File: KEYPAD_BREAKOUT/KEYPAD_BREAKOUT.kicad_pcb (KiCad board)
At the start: 4 copper layers, 46.7 x 76.6 mm, 21 parts, among them J1 Conn_01x14, SW0 SW_RGB, SW1 SW_RGB, SW2 SW_RGB, SW3 SW_RGB, SW4 SW_RGB, SW5 SW_RGB, SW6 SW_RGB, SW7 SW_RGB, SW8 SW_RGB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

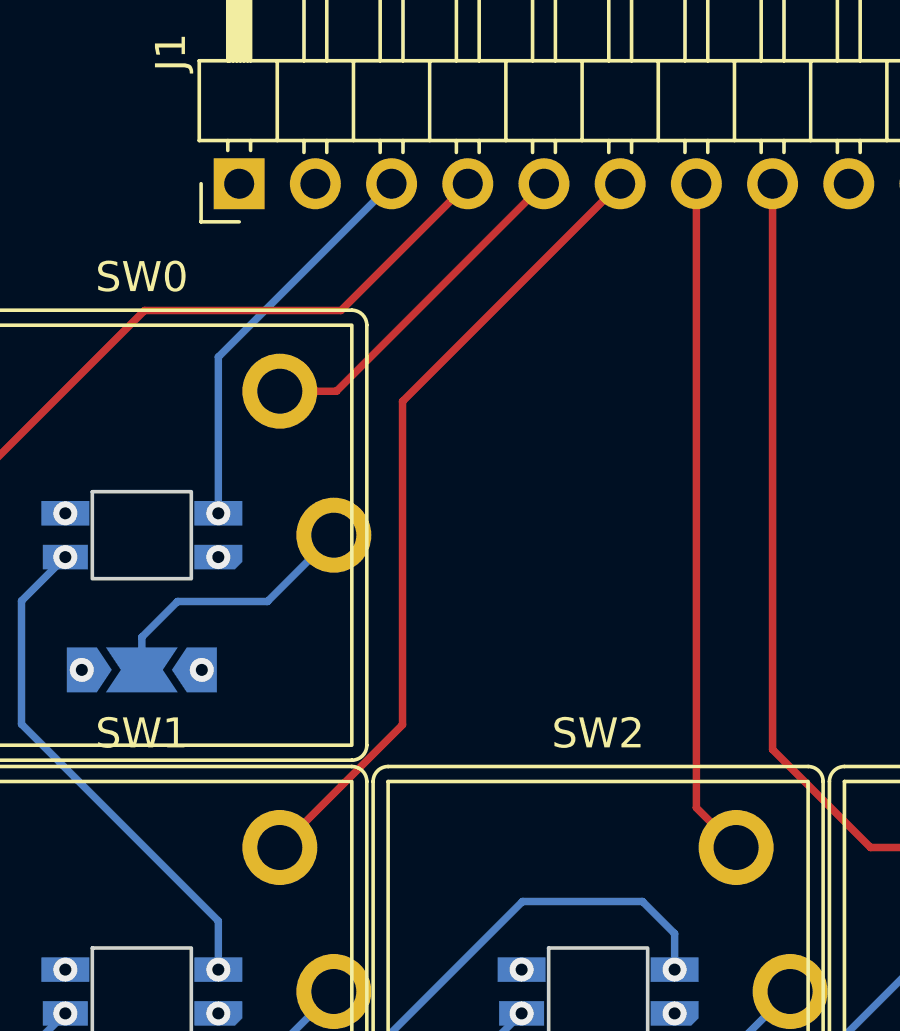
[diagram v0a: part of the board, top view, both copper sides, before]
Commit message: [KEYPAD_BREAKOUT] Minor trace adjust, readme update
Signed-off-by: Adam BZH <424778940z@users.noreply.github.com>
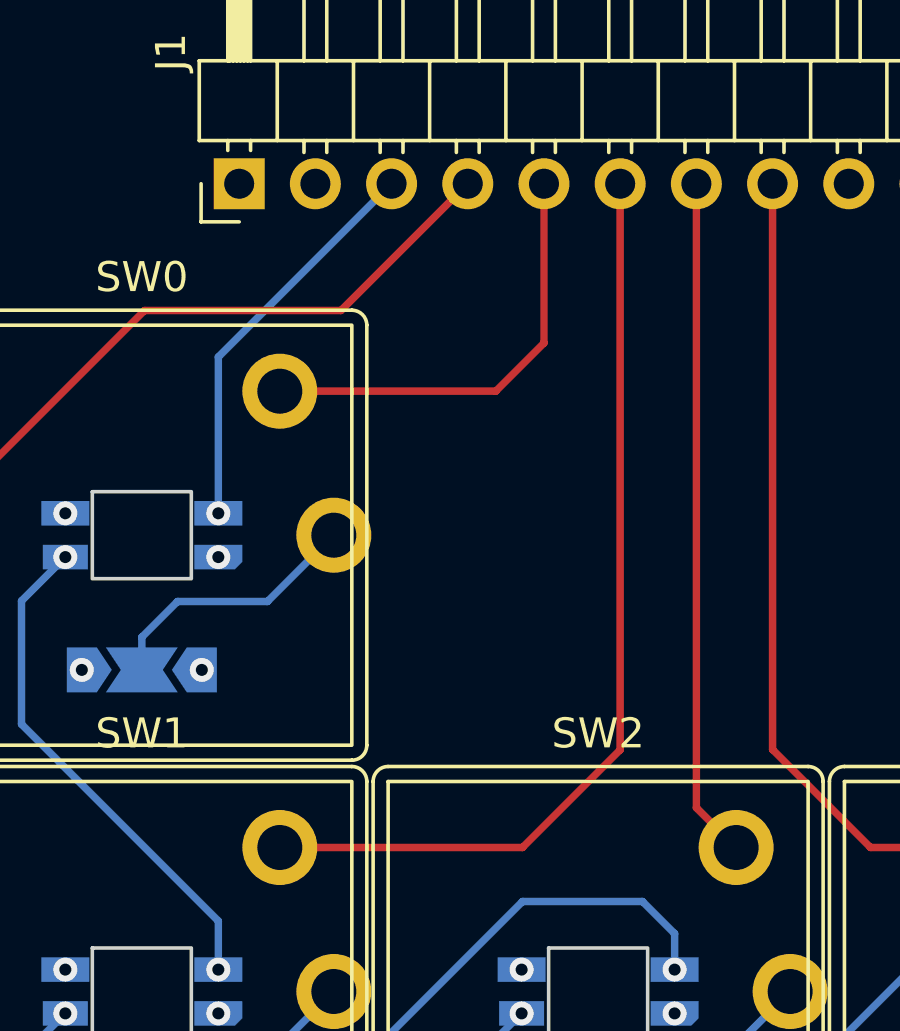
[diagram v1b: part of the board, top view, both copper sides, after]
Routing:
- net /SW1: track 26.8 -> 31.6 mm
- net /SW0: track 11.7 -> 14.8 mm
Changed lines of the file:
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@@
   (segment (start 139.25 100.65) (end 133.4 106.5) (width 0.25) (layer "F.Cu") (net 4))
   (via (at 140.88 100.65) (size 0.8) (drill 0.4) (layers "F.Cu" "B.Cu") (net 4))
-  (segment (start 117.61 49.49) (end 119.5 49.49) (width 0.25) (layer "F.Cu") (net 5))
-  (segment (start 119.5 49.49) (end 126.415 42.575) (width 0.25) (layer "F.Cu") (net 5))
-  (segment (start 121.7 49.83) (end 128.955 42.575) (width 0.25) (layer "F.Cu") (net 6))
-  (segment (start 121.7 60.61) (end 121.7 49.83) (width 0.25) (layer "F.Cu") (net 6))
-  (segment (start 117.61 64.7) (end 121.7 60.61) (width 0.25) (layer "F.Cu") (net 6))
+  (segment (start 126.415 47.885) (end 126.415 42.575) (width 0.25) (layer "F.Cu") (net 5))
+  (segment (start 117.61 49.49) (end 124.81 49.49) (width 0.25) (layer "F.Cu") (net 5))
+  (segment (start 124.81 49.49) (end 126.415 47.885) (width 0.25) (layer "F.Cu") (net 5))
+  (segment (start 125.7 64.7) (end 128.955 61.445) (width 0.25) (layer "F.Cu") (net 6))
+  (segment (start 117.61 64.7) (end 125.7 64.7) (width 0.25) (layer "F.Cu") (net 6))
+  (segment (start 128.955 61.445) (end 128.955 42.575) (width 0.25) (layer "F.Cu") (net 6))
   (segment (start 131.495 63.375) (end 131.495 42.575) (width 0.25) (layer "F.Cu") (net 7))
   (segment (start 132.82 64.7) (end 131.495 63.375) (width 0.25) (layer "F.Cu") (net 7))
@@
   (segment (start 148.03 79.91) (end 148.03 67.93) (width 0.25) (layer "In1.Cu") (net 11))
   (segment (start 141.655 61.555) (end 141.655 42.575) (width 0.25) (layer "In1.Cu") (net 11))
+  (segment (start 122.5 67.9) (end 144.195 46.205) (width 0.25) (layer "In2.Cu") (net 12))
+  (segment (start 144.195 46.205) (end 144.195 42.575) (width 0.25) (layer "In2.Cu") (net 12))
+  (segment (start 122.5 90.23) (end 122.5 67.9) (width 0.25) (layer "In2.Cu") (net 12))
   (segment (start 117.61 95.12) (end 122.5 90.23) (width 0.25) (layer "In2.Cu") (net 12))
-  (segment (start 122.5 90.23) (end 122.5 64.27) (width 0.25) (layer "In2.Cu") (net 12))
-  (segment (start 122.5 64.27) (end 144.195 42.575) (width 0.25) (layer "In2.Cu") (net 12))
+  (segment (start 132.82 83.28) (end 137 79.1) (width 0.25) (layer "In2.Cu") (net 13))
+  (segment (start 146.735 51.265) (end 146.735 42.575) (width 0.25) (layer "In2.Cu") (net 13))
+  (segment (start 137 61) (end 146.735 51.265) (width 0.25) (layer "In2.Cu") (net 13))
   (segment (start 132.82 95.12) (end 132.82 83.28) (width 0.25) (layer "In2.Cu") (net 13))
-  (segment (start 137 79.1) (end 137 52.31) (width 0.25) (layer "In2.Cu") (net 13))
-  (segment (start 137 52.31) (end 146.735 42.575) (width 0.25) (layer "In2.Cu") (net 13))
-  (segment (start 132.82 83.28) (end 137 79.1) (width 0.25) (layer "In2.Cu") (net 13))
-  (segment (start 150.1 45.6) (end 149.275 44.775) (width 0.25) (layer "In2.Cu") (net 14))
-  (segment (start 149.275 44.775) (end 149.275 42.575) (width 0.25) (layer "In2.Cu") (net 14))
+  (segment (start 137 79.1) (end 137 61) (width 0.25) (layer "In2.Cu") (net 13))
+  (segment (start 150.1 63.1) (end 149.275 62.275) (width 0.25) (layer "In2.Cu") (net 14))
+  (segment (start 150 75.6) (end 148 73.6) (width 0.25) (layer "In2.Cu") (net 14))
+  (segment (start 150 81.1) (end 150 75.6) (width 0.25) (layer "In2.Cu") (net 14))
+  (segment (start 150.1 65.9) (end 150.1 63.1) (width 0.25) (layer "In2.Cu") (net 14))
+  (segment (start 148.03 95.12) (end 148.03 83.07) (width 0.25) (layer "In2.Cu") (net 14))
+  (segment (start 148 68) (end 150.1 65.9) (width 0.25) (layer "In2.Cu") (net 14))
   (segment (start 148 73.6) (end 148 68) (width 0.25) (layer "In2.Cu") (net 14))
-  (segment (start 148 68) (end 150.1 65.9) (width 0.25) (layer "In2.Cu") (net 14))
   (segment (start 148.03 83.07) (end 150 81.1) (width 0.25) (layer "In2.Cu") (net 14))
-  (segment (start 150 81.1) (end 150 75.6) (width 0.25) (layer "In2.Cu") (net 14))
-  (segment (start 150 75.6) (end 148 73.6) (width 0.25) (layer "In2.Cu") (net 14))
-  (segment (start 150.1 65.9) (end 150.1 45.6) (width 0.25) (layer "In2.Cu") (net 14))
-  (segment (start 148.03 95.12) (end 148.03 83.07) (width 0.25) (layer "In2.Cu") (net 14))
+  (segment (start 149.275 62.275) (end 149.275 42.575) (width 0.25) (layer "In2.Cu") (net 14))
   (segment (start 114.2 71.71) (end 113.01 72.9) (width 0.25) (layer "B.Cu") (net 15))
   (segment (start 117.2 71.71) (end 114.2 71.71) (width 0.25) (layer "B.Cu") (net 15))

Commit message: [KEYPAD_BREAKOUT] Version 1 release, multiple fixes
Signed-off-by: Adam BZH <424778940z@users.noreply.github.com>
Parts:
- added J0: Conn_01x14, Connector_PinHeader_2.54mm:PinHeader_1x14_P2.54mm_Horizontal, F.Cu at (116.3, 42.6)
- J1: footprint Connector_PinHeader_2.54mm:PinHeader_1x14_P2.54mm_Horizontal -> Connector_PinSocket_2.00mm:PinSocket_2x07_P2.00mm_Vertical_SMD
- moved J1 22.8 mm to (135.4, 55.0)
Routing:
- net /VCC: track 0.00 -> 317.5 mm
- net /DOUT: track 109.4 -> 150.8 mm, vias 1 -> 2
- net /SW1: track 31.6 -> 50.4 mm
- net /SW9: track 55.4 -> 74.2 mm
- net /SW7: track 63.6 -> 81.1 mm
- net /DIN: track 13.4 -> 30.6 mm, vias 1 -> 0
- net /SW3: track 34.2 -> 51.2 mm
- net /SW5: track 39.9 -> 56.2 mm
- net /SW0: track 14.8 -> 28.1 mm
- net /SW8: track 58.3 -> 69.8 mm
- net /SW2: track 22.7 -> 33.6 mm
- net /SW6: track 40.0 -> 50.2 mm
- net /SW4: track 45.2 -> 54.8 mm
- net Net-(SW6-DOUT): track 31.0 -> 30.8 mm, vias 2 -> 0
- net Net-(SW3-DOUT): track 31.0 -> 30.8 mm, vias 2 -> 0
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- added copper zone on In1.Cu, net /GND
- removed copper zone on In1.Cu, net /VCC
